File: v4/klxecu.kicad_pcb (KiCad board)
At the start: 4 copper layers, 99.7 x 99.7 mm, 70 parts, among them IC1 SP721, J1 cam_sensor, J2 Conn_01x06, J3 DIP8, J4 Conn_02x04_Counter_Clockwise, J5 IGN_ARD_OUT, J7 IGN_CONN, J8 TACH_OUT, Q1 SSM3K357R, Q2 SSM3K357R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

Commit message: V4 potential design
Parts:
- added J6: Conn_01x01_Male, Connector_PinHeader_2.54mm:PinHeader_1x01_P2.54mm_Vertical, F.Cu at (128.9, 40.6)
- added J9: Conn_01x01_Male, Connector_PinHeader_2.54mm:PinHeader_1x01_P2.54mm_Vertical, F.Cu at (125.1, 40.6)
- added JP10: SolderJumper_2_Open, Jumper:SolderJumper-2_P1.3mm_Open_RoundedPad1.0x1.5mm, F.Cu at (106.7, 48.9)
- added JP11: SolderJumper_2_Open, Jumper:SolderJumper-2_P1.3mm_Open_RoundedPad1.0x1.5mm, F.Cu at (106.7, 44.5)
- added JP12: SolderJumper_2_Open, Jumper:SolderJumper-2_P1.3mm_Open_RoundedPad1.0x1.5mm, F.Cu at (120.7, 41.3)
- added JP8: SolderJumper_2_Open, Jumper:SolderJumper-2_P1.3mm_Open_RoundedPad1.0x1.5mm, F.Cu at (101.6, 44.5)
- added JP9: SolderJumper_2_Open, Jumper:SolderJumper-2_P1.3mm_Open_RoundedPad1.0x1.5mm, F.Cu at (101.6, 48.9)
- added R3: 470, Resistor_THT:R_Axial_DIN0204_L3.6mm_D1.6mm_P5.08mm_Horizontal, F.Cu at (104.1, 102.2)
- added U5: 74HC4050, Package_DIP:DIP-16_W7.62mm_LongPads, F.Cu at (111.8, 52.1)
- moved Q1 242.3 mm to (86.4, 92.7), turned to 180 degrees
- moved J8 229.5 mm to (80.6, 108.6)
- moved Q4 229.1 mm to (91.4, 101.6), turned to 180 degrees
- moved Q6 223.5 mm to (91.4, 92.7), turned to 180 degrees
- moved R21 192.1 mm to (109.9, 107.3)
- moved D4 181.8 mm to (107.3, 101.6)
- moved D3 175.5 mm to (114.9, 97.8), turned to 180 degrees
- moved C18 70.5 mm to (127.0, 94.7), turned to -90 degrees
- moved R15 59.9 mm to (123.8, 99.7), turned to 90 degrees
- moved R18 38.0 mm to (76.8, 100.3), turned to -90 degrees
- moved R19 36.8 mm to (74.3, 105.4), turned to 90 degrees
- moved C20 36.5 mm to (61.6, 98.4), turned to 180 degrees
- moved C19 35.2 mm to (67.3, 98.4), turned to 180 degrees
- moved U4 29.9 mm to (66.7, 102.2), turned to -90 degrees
- moved J7 27.6 mm to (55.2, 101.6)
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- renumbered JP4 to 22, JP3 to 22, JP5 to 24
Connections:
- D3 pad 2: CLUTCH-SW -> CLUTCH-ARD-D51
- D4 pad 1: CLUTCH-SW -> CLUTCH-ARD-D51
- J3 pad 2: KILL-SW -> Net-(J3-Pad2)
- J3 pad 3: SIDE-SW -> Net-(J3-Pad3)
- J3 pad 5: NEUTRAL -> Net-(J3-Pad5)
- J3 pad 6: VDOWN -> Net-(J3-Pad6)
- U3 pad D51: CLUTCH-SW -> CLUTCH-ARD-D51
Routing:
- net VSS: track 0.00 -> 139.7 mm, vias 0 -> 7
- net KILL-SW: track 0.00 -> 128.3 mm, vias 0 -> 3
- net DIR-ARD-D16: track 0.00 -> 97.6 mm, vias 0 -> 2
- net STEP-ARD-D17: track 0.00 -> 97.2 mm, vias 0 -> 2
- net EN-ARD-D24: track 0.00 -> 91.1 mm, vias 0 -> 3
- net MIL: track 0.00 -> 87.5 mm, vias 0 -> 1
- net GND: track 77.5 -> 155.3 mm, vias 5 -> 6
- net TEMP-WARN: track 0.00 -> 74.7 mm, vias 0 -> 1
- net Net-(Q3-Pad1): track 0.00 -> 52.7 mm, vias 0 -> 1
- net Net-(J3-Pad6): track 0.00 -> 48.0 mm
- net Net-(J3-Pad5): track 0.00 -> 47.8 mm
- net +12V: track 117.4 -> 163.6 mm, vias 0 -> 1
- net AIRSW: track 20.5 -> 57.6 mm
- net FAN-RELAY: track 17.6 -> 54.3 mm
- net Net-(J8-Pad1): track 0.00 -> 33.7 mm
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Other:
- board size 99.7 x 99.7 mm -> 95.9 x 76.2 mm

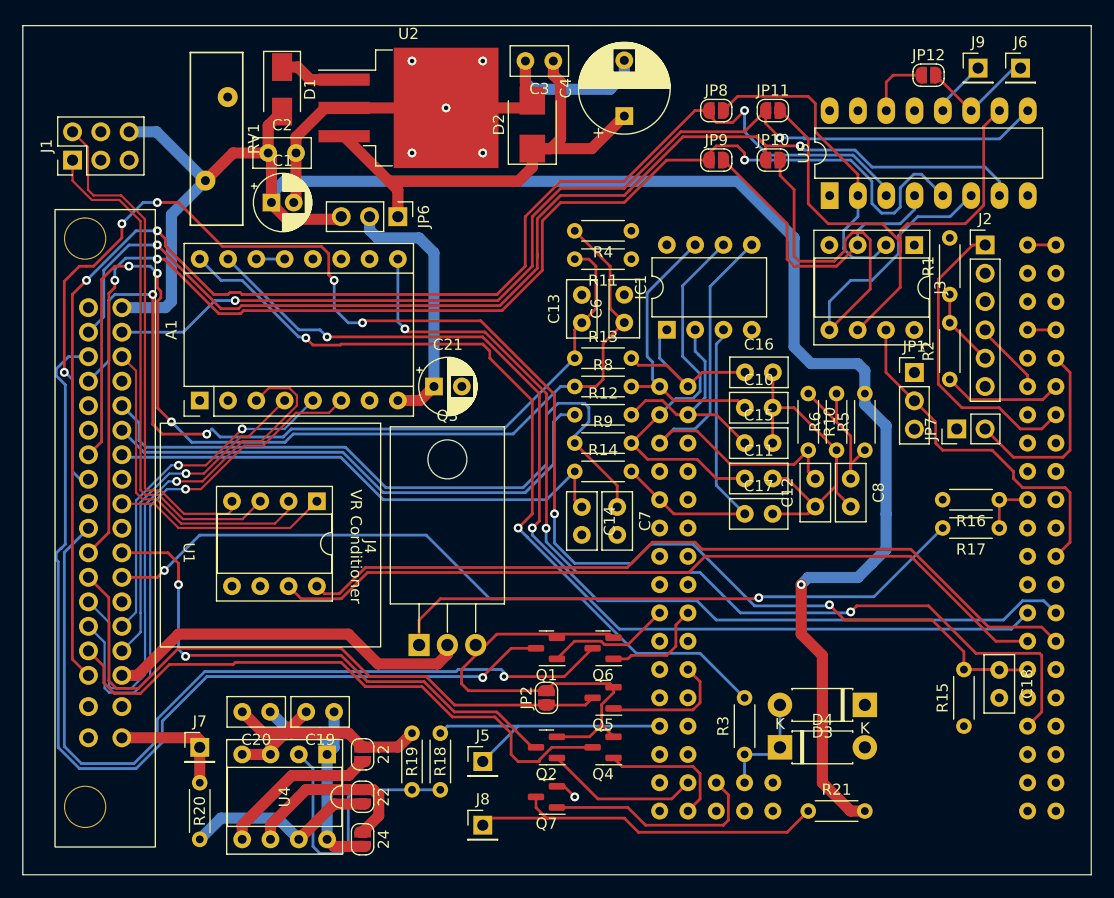
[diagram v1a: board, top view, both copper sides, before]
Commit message: Convert to a 2 layer board
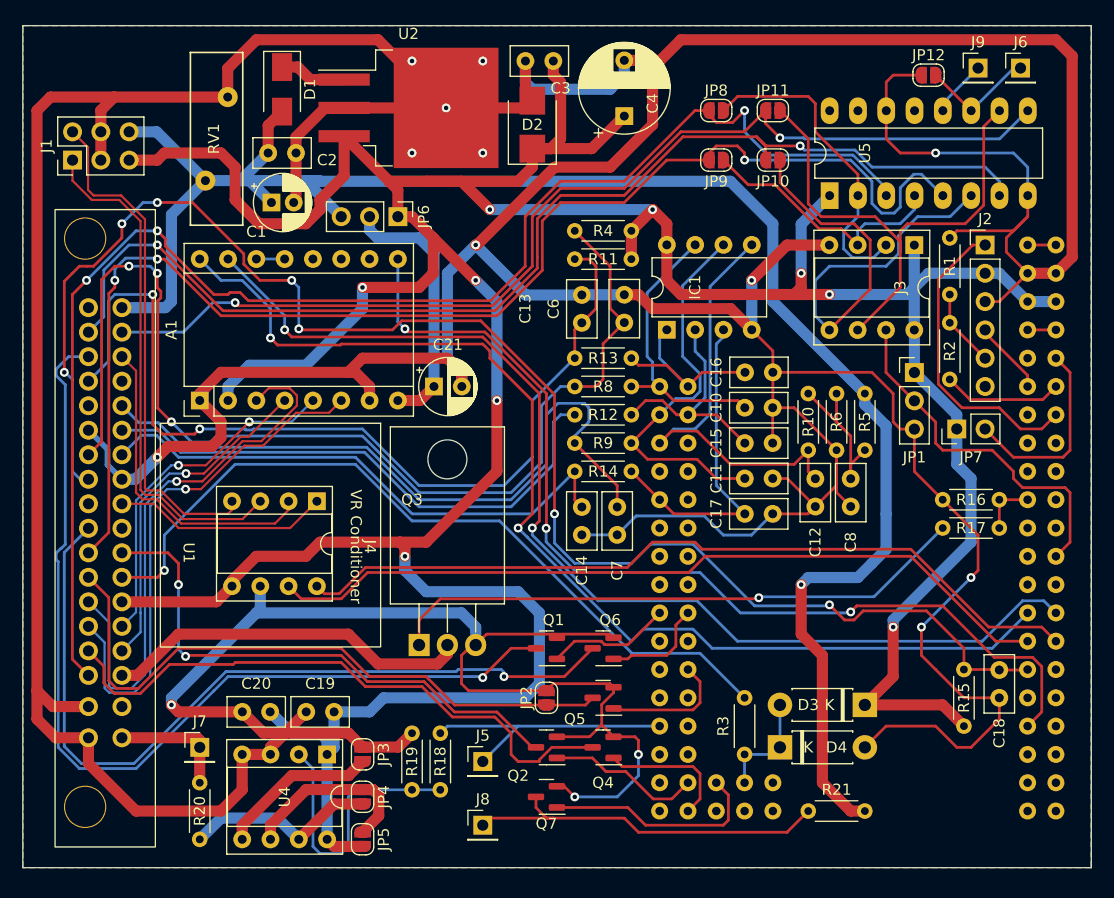
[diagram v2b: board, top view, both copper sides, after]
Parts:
- renumbered 22 to JP3, 22 to JP4, 24 to JP5
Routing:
- net GND: track 155.3 -> 673.0 mm, vias 6 -> 14
- net +5V: track 66.5 -> 370.6 mm, vias 0 -> 9
- net IAT: track 93.9 -> 101.0 mm
- net CLUTCH-SW: track 63.5 -> 70.6 mm
- net CLT: track 76.7 -> 83.3 mm
- net DIR-ARD-D16: track 97.6 -> 101.5 mm
- net Net-(J3-Pad3): track 27.1 -> 23.6 mm
- net Net-(J3-Pad5): track 47.8 -> 44.9 mm
- net O2S: track 46.8 -> 49.3 mm
- net STEP-ARD-D17: track 97.2 -> 99.5 mm
- net +12V: track 163.6 -> 161.4 mm
- net VSS: track 139.7 -> 141.2 mm
- net MIL: track 87.5 -> 86.3 mm
- net TEMP-WARN: track 74.7 -> 73.6 mm
- net MAP: track 48.1 -> 49.1 mm
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- added copper zone on B.Cu, net GND
- added copper zone on F.Cu, net GND
- removed copper zone on In2.Cu, net +5V
- removed copper zone on In1.Cu, net GND
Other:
- board size 95.9 x 76.2 mm -> 95.9 x 75.6 mm
- copper layers 4 -> 2
